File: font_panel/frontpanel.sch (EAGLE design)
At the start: 18 parts

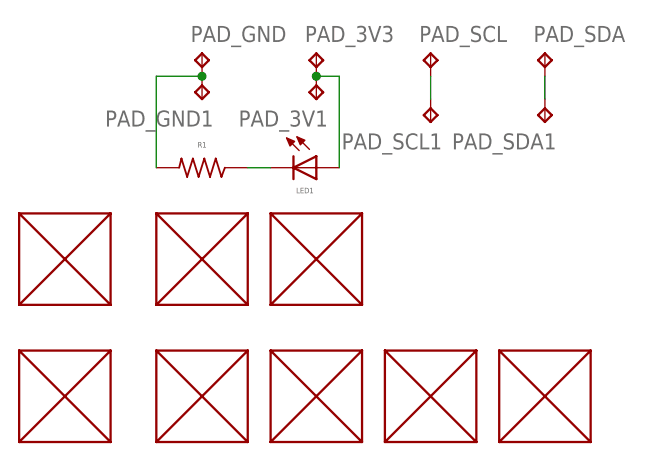
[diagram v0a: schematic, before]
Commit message: front panel initial modifications
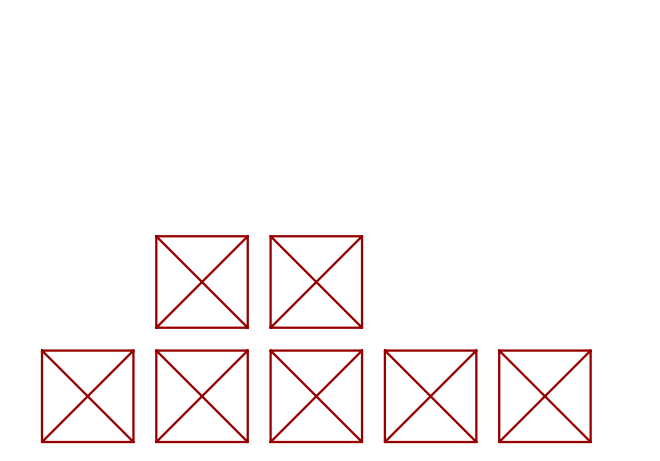
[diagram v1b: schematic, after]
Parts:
- removed LED1: (no value), Multischriever:LEDREVERSE
- removed PAD_3V1, PAD_3V3, PAD_GND, PAD_GND1, PAD_SCL, PAD_SCL1, PAD_SDA, PAD_SDA1: TPB1,27, testpad:TPB1,27
- removed R1: (no value), Multischriever:RESISTOR
- removed U$10: HOLESOLED, Multischriever:HOLESOLED
- removed U$9: HOLESROTARY, Multischriever:HOLESROTARY
- added U$2: HOLESLED_THROUGH_PCB, Multischriever:HOLESLED_THROUGH_PCB
- U$8: value HOLESUSBA -> HOLESLED_THROUGH_PCB; device Multischriever:HOLESUSBA -> Multischriever:HOLESLED_THROUGH_PCB
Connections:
- removed net 3V3: LED1.A, PAD_3V1.TP, PAD_3V3.TP
- removed net GND: PAD_GND.TP, PAD_GND1.TP, R1.2
- removed net N$3: LED1.C, R1.1
- removed net SCL: PAD_SCL.TP, PAD_SCL1.TP
- removed net SDA: PAD_SDA.TP, PAD_SDA1.TP
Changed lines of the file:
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@@
 <part name="U$5" library="Multischriever" deviceset="HOLES" device="RJ45_NOSHIELD" value="HOLESRJ45_NOSHIELD"/>
 <part name="U$6" library="Multischriever" deviceset="HOLES" device="RJ45"/>
-<part name="U$8" library="Multischriever" deviceset="HOLES" device="USBA"/>
-<part name="LED1" library="Multischriever" deviceset="LED" device="REVERSE"/>
-<part name="U$9" library="Multischriever" deviceset="HOLES" device="ROTARY"/>
-<part name="R1" library="Multischriever" deviceset="RESISTOR" device=""/>
-<part name="PAD_GND" library="testpad" library_urn="urn:adsk.eagle:library:385" deviceset="TP" device="B1,27" package3d_urn="urn:adsk.eagle:package:27944/1"/>
-<part name="PAD_3V3" library="testpad" library_urn="urn:adsk.eagle:library:385" deviceset="TP" device="B1,27" package3d_urn="urn:adsk.eagle:package:27944/1"/>
-<part name="PAD_SCL" library="testpad" library_urn="urn:adsk.eagle:library:385" deviceset="TP" device="B1,27" package3d_urn="urn:adsk.eagle:package:27944/1"/>
-<part name="PAD_SDA" library="testpad" library_urn="urn:adsk.eagle:library:385" deviceset="TP" device="B1,27" package3d_urn="urn:adsk.eagle:package:27944/1"/>
-<part name="U$10" library="Multischriever" deviceset="HOLES" device="OLED"/>
-<part name="PAD_GND1" library="testpad" library_urn="urn:adsk.eagle:library:385" deviceset="TP" device="B1,27" package3d_urn="urn:adsk.eagle:package:27944/1"/>
-<part name="PAD_3V1" library="testpad" library_urn="urn:adsk.eagle:library:385" deviceset="TP" device="B1,27" package3d_urn="urn:adsk.eagle:package:27944/1"/>
-<part name="PAD_SCL1" library="testpad" library_urn="urn:adsk.eagle:library:385" deviceset="TP" device="B1,27" package3d_urn="urn:adsk.eagle:package:27944/1"/>
-<part name="PAD_SDA1" library="testpad" library_urn="urn:adsk.eagle:library:385" deviceset="TP" device="B1,27" package3d_urn="urn:adsk.eagle:package:27944/1"/>
+<part name="U$2" library="Multischriever" deviceset="HOLES" device="LED_THROUGH_PCB"/>
+<part name="U$8" library="Multischriever" deviceset="HOLES" device="LED_THROUGH_PCB"/>
 </parts>
 <sheets>
@@
 </plain>
 <instances>
-<instance part="U$1" gate="G$1" x="2.54" y="30.48" smashed="yes"/>
+<instance part="U$1" gate="G$1" x="5.08" y="15.24" smashed="yes"/>
 <instance part="U$3" gate="G$1" x="17.78" y="15.24" smashed="yes"/>
 <instance part="U$4" gate="G$1" x="30.48" y="15.24" smashed="yes"/>
 <instance part="U$5" gate="G$1" x="43.18" y="15.24" smashed="yes"/>
 <instance part="U$6" gate="G$1" x="55.88" y="15.24" smashed="yes"/>
-<instance part="U$8" gate="G$1" x="30.48" y="30.48" smashed="yes"/>
-<instance part="LED1" gate="G$1" x="30.48" y="40.64" smashed="yes" rot="R270">
-<attribute name="NAME" x="29.21" y="38.1" size="0.6096" layer="95" align="center"/>
-<attribute name="VALUE" x="29.21" y="36.83" size="0.6096" layer="96" align="center"/>
-</instance>
-<instance part="U$9" gate="G$1" x="2.54" y="15.24" smashed="yes"/>
-<instance part="R1" gate="G$1" x="17.78" y="40.64" smashed="yes" rot="R180">
-<attribute name="NAME" x="17.78" y="43.18" size="0.6096" layer="95" rot="R180" align="center"/>
-<attribute name="VALUE" x="17.78" y="44.45" size="0.6096" layer="96" rot="R180" align="center"/>
-</instance>
-<instance part="PAD_GND" gate="G$1" x="17.78" y="53.34" smashed="yes">
-<attribute name="NAME" x="16.51" y="54.61" size="1.778" layer="95"/>
-<attribute name="TP_SIGNAL_NAME" x="19.05" y="52.07" size="1.778" layer="97"/>
-</instance>
-<instance part="PAD_3V3" gate="G$1" x="30.48" y="53.34" smashed="yes">
-<attribute name="NAME" x="29.21" y="54.61" size="1.778" layer="95"/>
-<attribute name="TP_SIGNAL_NAME" x="31.75" y="52.07" size="1.778" layer="97"/>
-</instance>
-<instance part="PAD_SCL" gate="G$1" x="43.18" y="53.34" smashed="yes">
-<attribute name="NAME" x="41.91" y="54.61" size="1.778" layer="95"/>
-<attribute name="TP_SIGNAL_NAME" x="44.45" y="52.07" size="1.778" layer="97"/>
-</instance>
-<instance part="PAD_SDA" gate="G$1" x="55.88" y="53.34" smashed="yes">
-<attribute name="NAME" x="54.61" y="54.61" size="1.778" layer="95"/>
-<attribute name="TP_SIGNAL_NAME" x="57.15" y="52.07" size="1.778" layer="97"/>
-</instance>
-<instance part="U$10" gate="G$1" x="17.78" y="30.48" smashed="yes"/>
-<instance part="PAD_GND1" gate="G$1" x="17.78" y="48.26" smashed="yes" rot="R180">
-<attribute name="NAME" x="19.05" y="46.99" size="1.778" layer="95" rot="R180"/>
-<attribute name="TP_SIGNAL_NAME" x="16.51" y="49.53" size="1.778" layer="97" rot="R180"/>
-</instance>
-<instance part="PAD_3V1" gate="G$1" x="30.48" y="48.26" smashed="yes" rot="R180">
-<attribute name="NAME" x="31.75" y="46.99" size="1.778" layer="95" rot="R180"/>
-<attribute name="TP_SIGNAL_NAME" x="29.21" y="49.53" size="1.778" layer="97" rot="R180"/>
-</instance>
-<instance part="PAD_SCL1" gate="G$1" x="43.18" y="45.72" smashed="yes" rot="R180">
-<attribute name="NAME" x="44.45" y="44.45" size="1.778" layer="95" rot="R180"/>
-<attribute name="TP_SIGNAL_NAME" x="41.91" y="46.99" size="1.778" layer="97" rot="R180"/>
-</instance>
-<instance part="PAD_SDA1" gate="G$1" x="55.88" y="45.72" smashed="yes" rot="R180">
-<attribute name="NAME" x="57.15" y="44.45" size="1.778" layer="95" rot="R180"/>
-<attribute name="TP_SIGNAL_NAME" x="54.61" y="46.99" size="1.778" layer="97" rot="R180"/>
-</instance>
+<instance part="U$2" gate="G$1" x="17.78" y="27.94" smashed="yes"/>
+<instance part="U$8" gate="G$1" x="30.48" y="27.94" smashed="yes"/>
 </instances>
 <busses>
 </busses>
 <nets>
-<net name="GND" class="0">
-<segment>
-<pinref part="PAD_GND" gate="G$1" pin="TP"/>
-<pinref part="PAD_GND1" gate="G$1" pin="TP"/>
-<pinref part="R1" gate="G$1" pin="2"/>
-<wire x1="12.7" y1="40.64" x2="12.7" y2="50.8" width="0.1524" layer="91"/>
-<wire x1="12.7" y1="50.8" x2="17.78" y2="50.8" width="0.1524" layer="91"/>
-<junction x="17.78" y="50.8"/>
-</segment>
-</net>
-<net name="3V3" class="0">
-<segment>
-<pinref part="PAD_3V3" gate="G$1" pin="TP"/>
-<pinref part="PAD_3V1" gate="G$1" pin="TP"/>
-<wire x1="30.48" y1="50.8" x2="33.02" y2="50.8" width="0.1524" layer="91"/>
-<junction x="30.48" y="50.8"/>
-<pinref part="LED1" gate="G$1" pin="A"/>
-<wire x1="33.02" y1="50.8" x2="33.02" y2="40.64" width="0.1524" layer="91"/>
-</segment>
-</net>
-<net name="SCL" class="0">
-<segment>
-<pinref part="PAD_SCL" gate="G$1" pin="TP"/>
-<pinref part="PAD_SCL1" gate="G$1" pin="TP"/>
-<wire x1="43.18" y1="48.26" x2="43.18" y2="50.8" width="0.1524" layer="91"/>
-</segment>
-</net>
-<net name="SDA" class="0">
-<segment>
-<pinref part="PAD_SDA" gate="G$1" pin="TP"/>
-<pinref part="PAD_SDA1" gate="G$1" pin="TP"/>
-<wire x1="55.88" y1="48.26" x2="55.88" y2="50.8" width="0.1524" layer="91"/>
-</segment>
-</net>
-<net name="N$3" class="0">
-<segment>
-<pinref part="R1" gate="G$1" pin="1"/>
-<pinref part="LED1" gate="G$1" pin="C"/>
-<wire x1="22.86" y1="40.64" x2="25.4" y2="40.64" width="0.1524" layer="91"/>
-</segment>
-</net>
 </nets>
 </sheet>
@@
 </schematic>
 </drawing>
-<compatibility>
-<note version="8.2" severity="warning">
-Since Version 8.2, EAGLE supports online libraries. The ids
-of those online libraries will not be understood (or retained)
-with this version.
-</note>
-<note version="8.3" severity="warning">
-Since Version 8.3, EAGLE supports URNs for individual library
-assets (packages, symbols, and devices). The URNs of those assets
-will not be understood (or retained) with this version.
-</note>
-<note version="8.3" severity="warning">
-Since Version 8.3, EAGLE supports the association of 3D packages
-with devices in libraries, schematics, and board files. Those 3D
-packages will not be understood (or retained) with this version.
-</note>
-</compatibility>
 </eagle>
